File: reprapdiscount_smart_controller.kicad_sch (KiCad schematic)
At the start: 17 parts, among them Q1 BC817, U1 74HC4050, U2 MIC5209

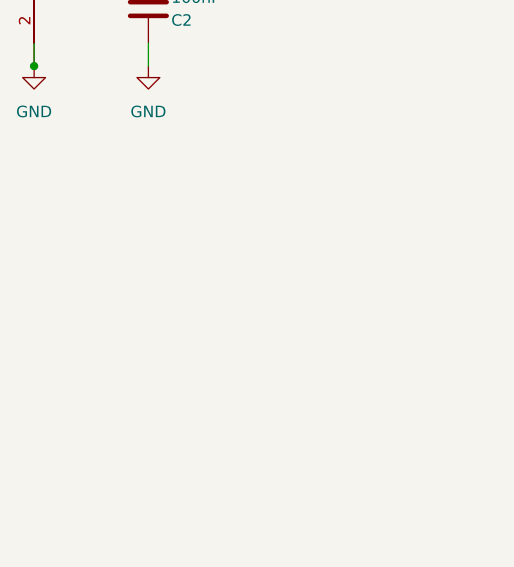
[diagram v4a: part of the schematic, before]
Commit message: fixup: restore mounting holes lost during cleanup
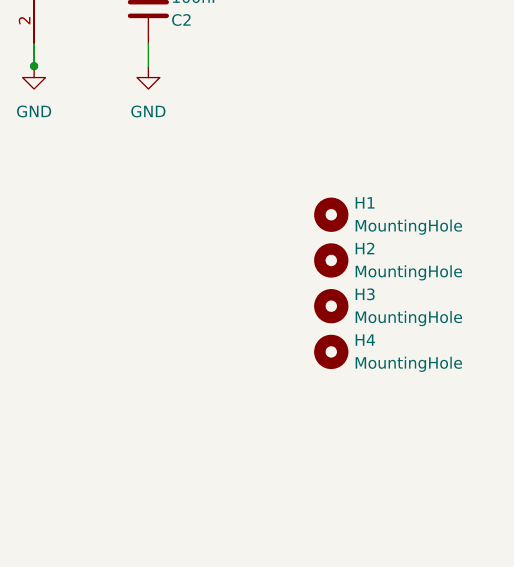
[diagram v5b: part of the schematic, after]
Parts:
- added H1, H2, H3, H4: MountingHole, reprapdiscount_smart_controller:MountingHole_3mm, symbol Mechanical:MountingHole
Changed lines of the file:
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@@
+    )
+  )
+  (symbol (lib_id "Mechanical:MountingHole") (at 233.68 87.63 0) (unit 1)
+    (in_bom yes) (on_board yes) (dnp no) (fields_autoplaced)
+    (property "Reference" "H4" (at 236.22 86.36 0)
+      (effects (font (size 1.27 1.27)) (justify left))
+    )
+    (property "Value" "MountingHole" (at 236.22 88.9 0)
+      (effects (font (size 1.27 1.27)) (justify left))
+    )
+    (property "Footprint" "reprapdiscount_smart_controller:MountingHole_3mm" (at 233.68 87.63 0)
+      (effects (font (size 1.27 1.27)) hide)
+    )
+    (property "Datasheet" "~" (at 233.68 87.63 0)
+      (effects (font (size 1.27 1.27)) hide)
+    )
+    (instances
+      (project "reprapdiscount_smart_controller"
+        (path "/c20eb3f6-d157-43e2-84ab-82664a430dd1"
+          (reference "H4") (unit 1)
+        )
+      )
     )
   )
@@
     )
   )
+  (symbol (lib_id "Mechanical:MountingHole") (at 233.68 82.55 0) (unit 1)
+    (in_bom yes) (on_board yes) (dnp no) (fields_autoplaced)
+    (property "Reference" "H3" (at 236.22 81.28 0)
+      (effects (font (size 1.27 1.27)) (justify left))
+    )
+    (property "Value" "MountingHole" (at 236.22 83.82 0)
+      (effects (font (size 1.27 1.27)) (justify left))
+    )
+    (property "Footprint" "reprapdiscount_smart_controller:MountingHole_3mm" (at 233.68 82.55 0)
+      (effects (font (size 1.27 1.27)) hide)
+    )
+    (property "Datasheet" "~" (at 233.68 82.55 0)
+      (effects (font (size 1.27 1.27)) hide)
+    )
+    (instances
+      (project "reprapdiscount_smart_controller"
+        (path "/c20eb3f6-d157-43e2-84ab-82664a430dd1"
+          (reference "H3") (unit 1)
+        )
+      )
+    )
+  )
   (symbol (lib_id "Device:C") (at 187.96 49.53 180) (unit 1)
     (in_bom yes) (on_board yes) (dnp no)
@@
         )
       )
+    )
+  )
+  (symbol (lib_id "Mechanical:MountingHole") (at 233.68 72.39 0) (unit 1)
+    (in_bom yes) (on_board yes) (dnp no) (fields_autoplaced)
+    (property "Reference" "H1" (at 236.22 71.12 0)
+      (effects (font (size 1.27 1.27)) (justify left))
+    )
+    (property "Value" "MountingHole" (at 236.22 73.66 0)
+      (effects (font (size 1.27 1.27)) (justify left))
+    )
+    (property "Footprint" "reprapdiscount_smart_controller:MountingHole_3mm" (at 233.68 72.39 0)
+      (effects (font (size 1.27 1.27)) hide)
+    )
+    (property "Datasheet" "~" (at 233.68 72.39 0)
+      (effects (font (size 1.27 1.27)) hide)
+    )
+    (instances
+      (project "reprapdiscount_smart_controller"
+        (path "/c20eb3f6-d157-43e2-84ab-82664a430dd1"
+          (reference "H1") (unit 1)
+        )
+      )
+    )
+  )
+  (symbol (lib_id "Mechanical:MountingHole") (at 233.68 77.47 0) (unit 1)
+    (in_bom yes) (on_board yes) (dnp no) (fields_autoplaced)
+    (property "Reference" "H2" (at 236.22 76.2 0)
+      (effects (font (size 1.27 1.27)) (justify left))
+    )
+    (property "Value" "MountingHole" (at 236.22 78.74 0)
+      (effects (font (size 1.27 1.27)) (justify left))
+    )
+    (property "Footprint" "reprapdiscount_smart_controller:MountingHole_3mm" (at 233.68 77.47 0)
+      (effects (font (size 1.27 1.27)) hide)
+    )
+    (property "Datasheet" "~" (at 233.68 77.47 0)
+      (effects (font (size 1.27 1.27)) hide)
+    )
+    (instances
+      (project "reprapdiscount_smart_controller"
+        (path "/c20eb3f6-d157-43e2-84ab-82664a430dd1"
+          (reference "H2") (unit 1)
+        )
+      )

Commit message: fixup: fix reset button height
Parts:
- PB1: footprint Button_Switch_THT:SW_PUSH_6mm_H5mm -> Button_Switch_THT:SW_PUSH_6mm_H7.3mm
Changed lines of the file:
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@@
       (effects (font (size 1.27 1.27)) (justify left))
     )
-    (property "Footprint" "Button_Switch_THT:SW_PUSH_6mm_H5mm" (at 132.08 156.21 0)
+    (property "Footprint" "Button_Switch_THT:SW_PUSH_6mm_H7.3mm" (at 132.08 156.21 0)
       (effects (font (size 1.27 1.27)) hide)
     )

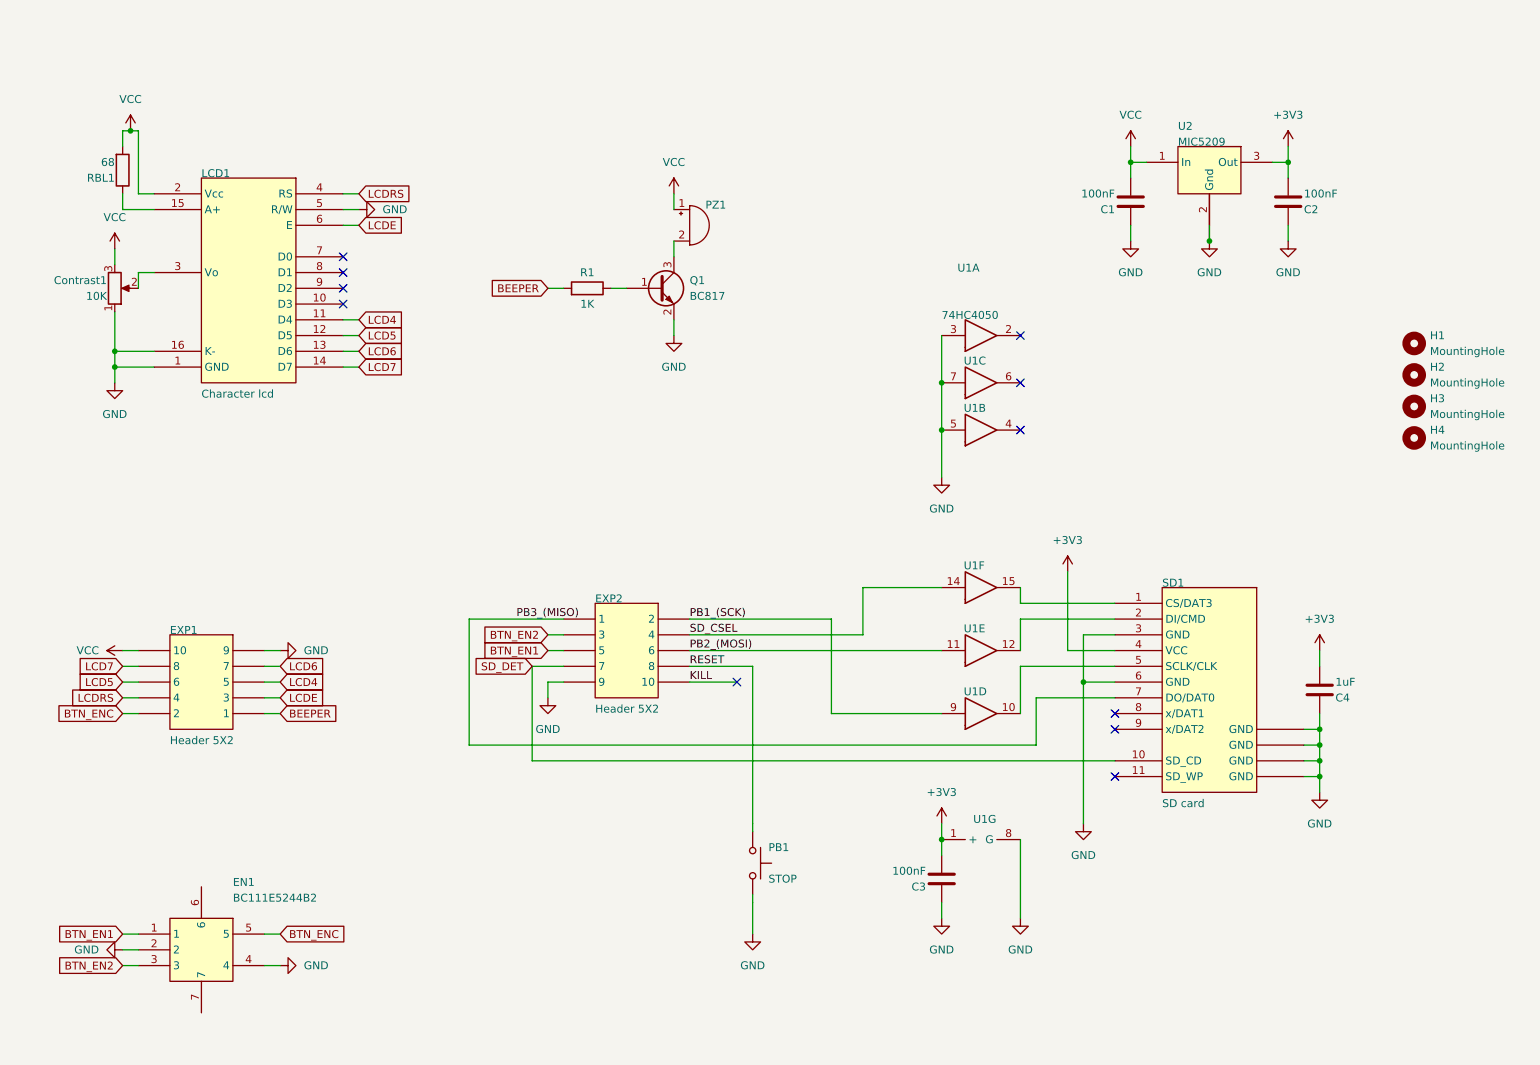
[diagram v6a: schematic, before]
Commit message: feature: add parts from ldo-rrlcd-a007
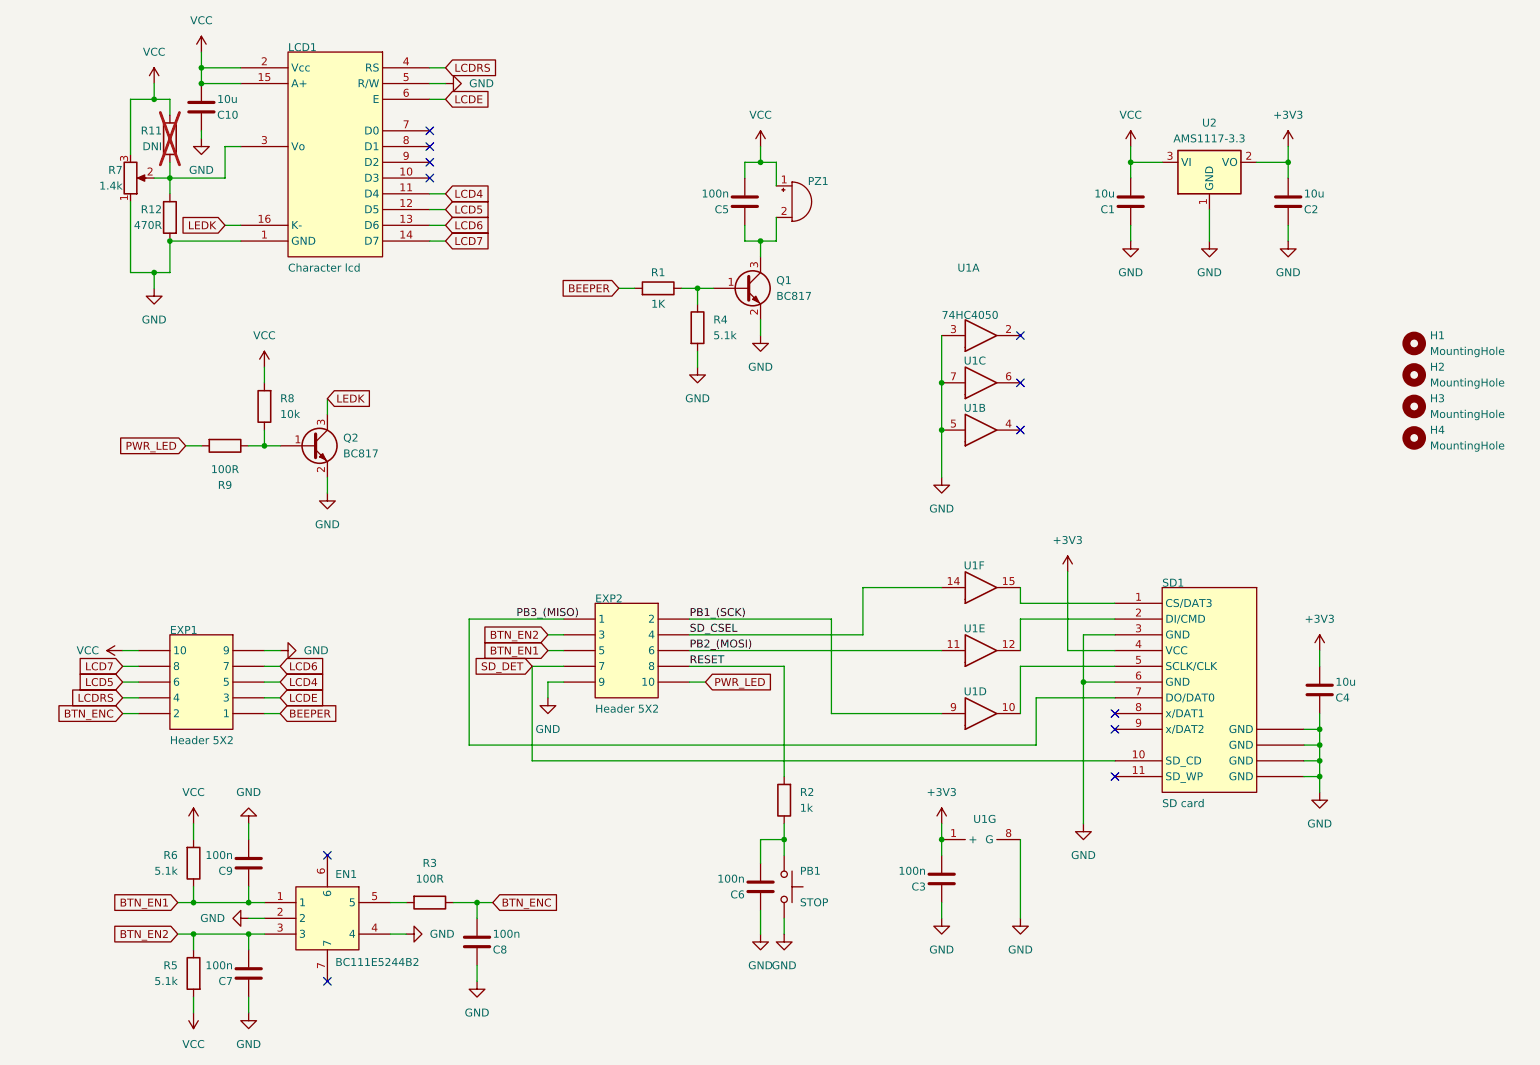
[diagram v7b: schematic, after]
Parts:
- removed RBL1: 68, Resistor_SMD:R_1206_3216Metric_Pad1.30x1.75mm_HandSolder, symbol Device:R
- removed U2: MIC5209, Package_TO_SOT_SMD:SOT-223, symbol reprapdiscount_smart_controller-altium-import:root_0_MIC5209
- added C10: 10u, Capacitor_SMD:C_0805_2012Metric_Pad1.18x1.45mm_HandSolder, symbol Device:C
- added C5, C6, C7, C8, C9: 100n, Capacitor_SMD:C_0805_2012Metric_Pad1.18x1.45mm_HandSolder, symbol Device:C
- added Q2: BC817, Package_TO_SOT_SMD:SOT-23, symbol Transistor_BJT:BC817
- added R11: DNI, Resistor_SMD:R_0805_2012Metric_Pad1.20x1.40mm_HandSolder, symbol Device:R
- added R12: 470R, Resistor_SMD:R_0805_2012Metric_Pad1.20x1.40mm_HandSolder, symbol Device:R
- added R2: 1k, Resistor_SMD:R_0805_2012Metric_Pad1.20x1.40mm_HandSolder, symbol Device:R
- added R3, R9: 100R, Resistor_SMD:R_0805_2012Metric_Pad1.20x1.40mm_HandSolder, symbol Device:R
- added R4, R5, R6: 5.1k, Resistor_SMD:R_0805_2012Metric_Pad1.20x1.40mm_HandSolder, symbol Device:R
- added R8: 10k, Resistor_SMD:R_0805_2012Metric_Pad1.20x1.40mm_HandSolder, symbol Device:R
- added U2: AMS1117-3.3, Package_TO_SOT_SMD:SOT-223-3_TabPin2, symbol Regulator_Linear:AMS1117-3.3
- C1, C2: value 100nF -> 10u
- C3: value 100nF -> 100n
- C4: value 1uF -> 10u
- R7: renamed from Contrast1; value 10K -> 1.4k
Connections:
- net +3V3: now also U2.2 (VO)
- net BTN_EN1: now also C9.1, R6.1
- net BTN_EN2: now also C7.2, R5.1
- net BTN_ENC: now also C8.2, R3.1; no longer EN1.5
- net GND: now also C10.1, C6.1, C7.1, C8.1, C9.2, Q2.2 (E), R12.2, R4.2, U2.1 (GND); no longer LCD1.16 (K-)
- net RESET: now also R2.2; no longer PB1.1
- net VCC: now also LCD1.15 (A+), C10.2, C5.2, R11.1, R5.2, R6.2, R8.2, U2.3 (VI)
- net at LCD1.3 (Vo), R7.2: now also R11.2, R12.1
- net at Q1.1 (B), R1.1: now also R4.1
- net at PZ1.2 (+), Q1.3 (C): now also C5.1
- net KILL renamed PWR_LED
- net PWR_LED: now also R9.2
- new net: C6.2, PB1.1, R2.1
- new net: Q2.1 (B), R8.1, R9.1
- new net: EN1.5, R3.2
- new net LEDK: LCD1.16 (K-), Q2.3 (C)
- no-connect marks 11 -> 12
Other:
- moved on the sheet: EN1, LCD1, PB1, PZ1, Q1, R1, R7

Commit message: feature: add fiducials
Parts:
- added FID1, FID2: Fiducial, Fiducial:Fiducial_1mm_Mask2mm, symbol Mechanical:Fiducial
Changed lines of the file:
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@@
+    )
+  )
+  (symbol (lib_id "Mechanical:Fiducial") (at 233.68 92.71 0) (unit 1)
+    (in_bom yes) (on_board yes) (dnp no) (fields_autoplaced)
+    (property "Reference" "FID1" (at 236.22 91.44 0)
+      (effects (font (size 1.27 1.27)) (justify left))
+    )
+    (property "Value" "Fiducial" (at 236.22 93.98 0)
+      (effects (font (size 1.27 1.27)) (justify left))
+    )
+    (property "Footprint" "Fiducial:Fiducial_1mm_Mask2mm" (at 233.68 92.71 0)
+      (effects (font (size 1.27 1.27)) hide)
+    )
+    (property "Datasheet" "~" (at 233.68 92.71 0)
+      (effects (font (size 1.27 1.27)) hide)
+    )
+    (instances
+      (project "reprapdiscount_smart_controller"
+        (path "/c20eb3f6-d157-43e2-84ab-82664a430dd1"
+          (reference "FID1") (unit 1)
+        )
+      )
     )
   )
@@
         )
       )
+    )
+  )
+  (symbol (lib_id "Mechanical:Fiducial") (at 233.68 97.79 0) (unit 1)
+    (in_bom yes) (on_board yes) (dnp no) (fields_autoplaced)
+    (property "Reference" "FID2" (at 236.22 96.52 0)
+      (effects (font (size 1.27 1.27)) (justify left))
+    )
+    (property "Value" "Fiducial" (at 236.22 99.06 0)
+      (effects (font (size 1.27 1.27)) (justify left))
+    )
+    (property "Footprint" "Fiducial:Fiducial_1mm_Mask2mm" (at 233.68 97.79 0)
+      (effects (font (size 1.27 1.27)) hide)
+    )
+    (property "Datasheet" "~" (at 233.68 97.79 0)
+      (effects (font (size 1.27 1.27)) hide)
+    )
+    (instances
+      (project "reprapdiscount_smart_controller"
+        (path "/c20eb3f6-d157-43e2-84ab-82664a430dd1"
+          (reference "FID2") (unit 1)
+        )
+      )
